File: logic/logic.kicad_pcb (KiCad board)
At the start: 2 copper layers, 27 parts, among them J1 DIN41612_03x32_ABC, J2 Conn_02x05_Odd_Even, U1 TPIC6595, U2 TPIC6595, U3 TPIC6595, U4 TPIC6595, U5 TPIC6595, U6 TPIC6595, U7 TPIC6595, U8 TPIC6595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

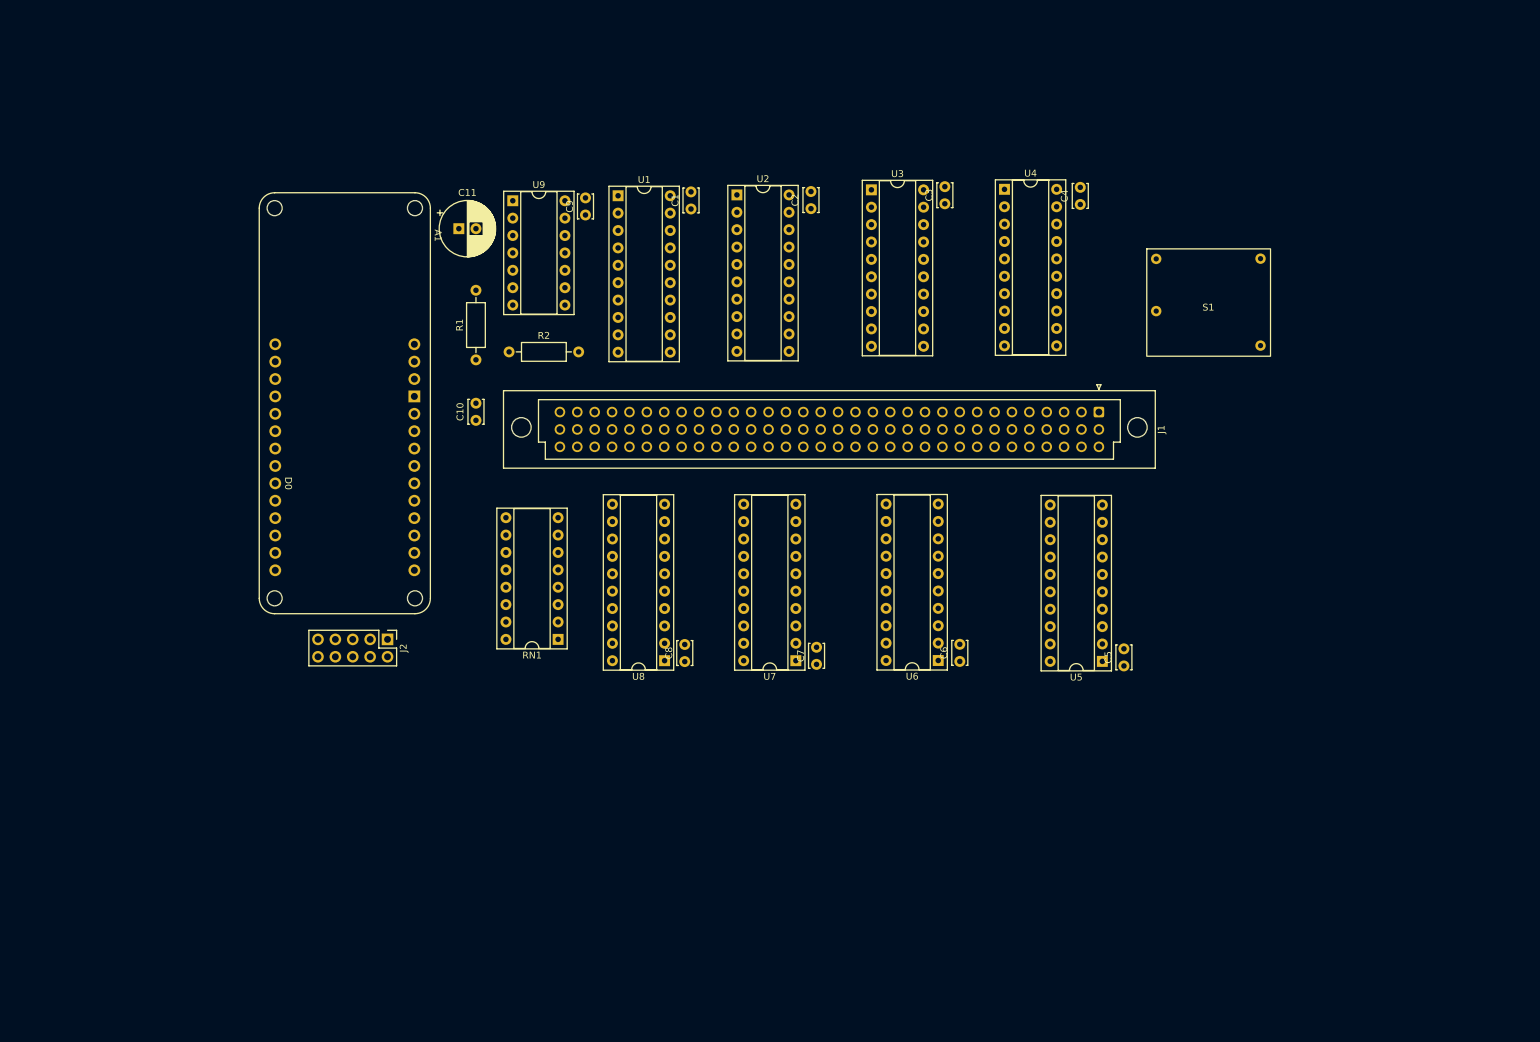
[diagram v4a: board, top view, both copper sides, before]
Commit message: Add low voltage supply to logic board
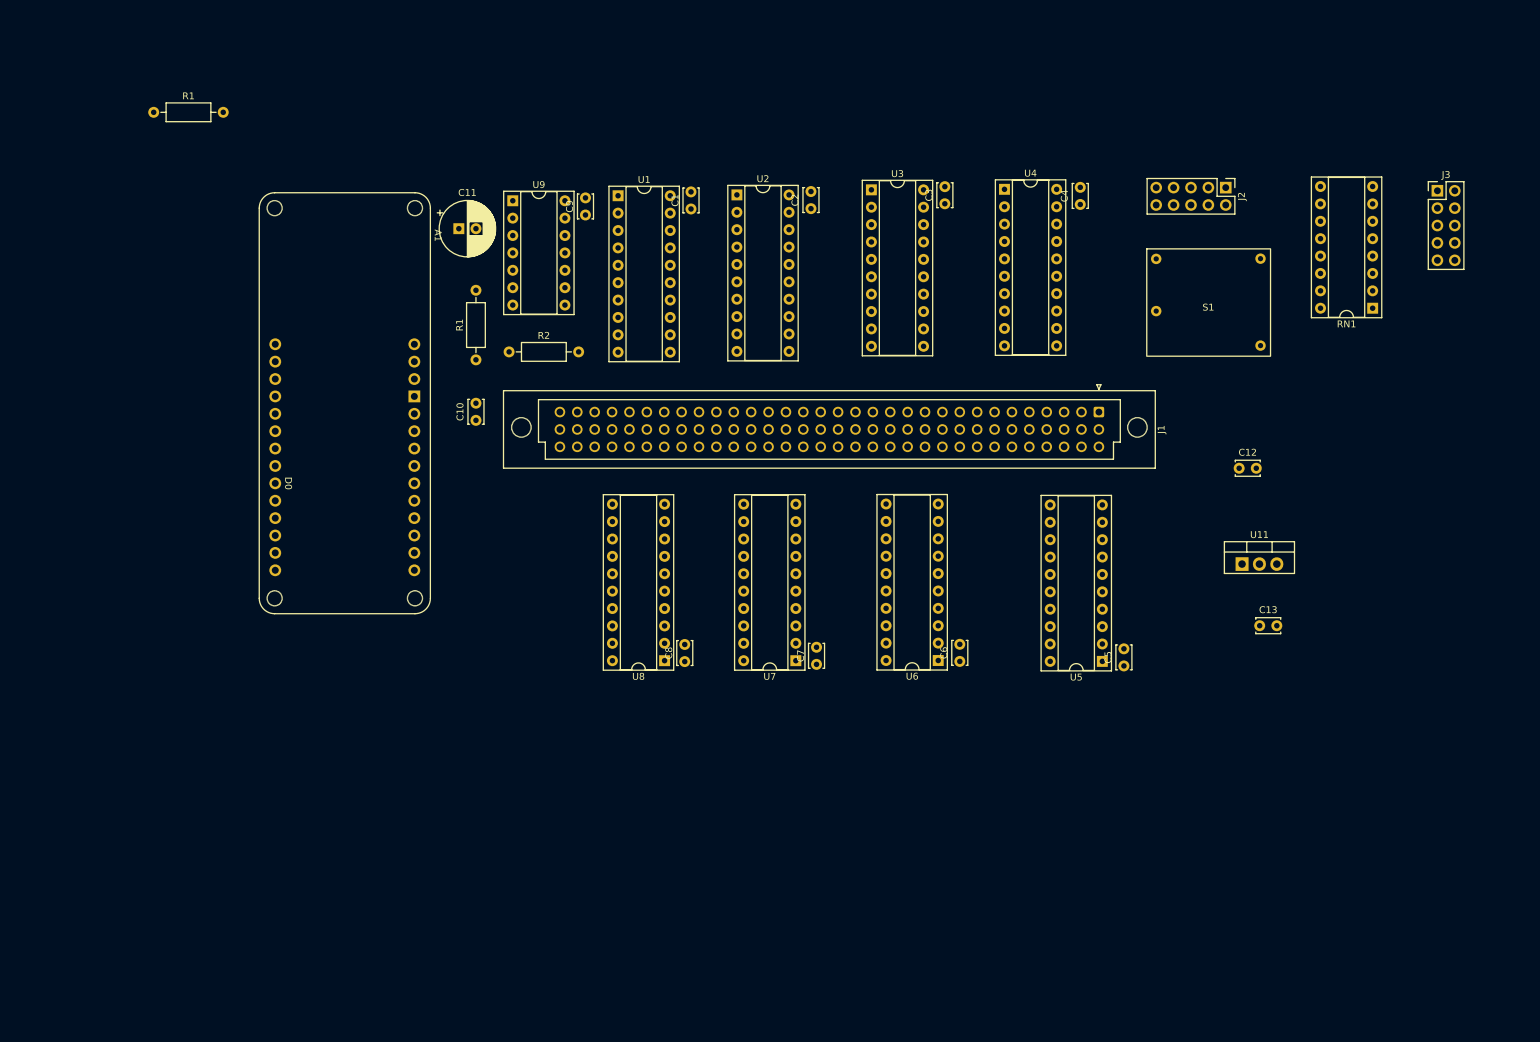
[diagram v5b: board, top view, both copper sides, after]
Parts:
- added C12: C, Capacitor_THT:C_Disc_D3.4mm_W2.1mm_P2.50mm, F.Cu at (214.5, 79.0)
- added C13: C, Capacitor_THT:C_Disc_D3.4mm_W2.1mm_P2.50mm, F.Cu at (217.5, 102.0)
- added J3: Conn_02x05_Odd_Even, Connector_PinHeader_2.54mm:PinHeader_2x05_P2.54mm_Vertical, F.Cu at (243.5, 38.5)
- added R1: R, Resistor_THT:R_Axial_DIN0207_L6.3mm_D2.5mm_P10.16mm_Horizontal, F.Cu at (55.9, 27.0)
- added U11: LM7805_TO220, Package_TO_SOT_THT:TO-220-3_Vertical, F.Cu at (214.9, 93.0)
- moved J2 139.1 mm to (212.5, 38.0)
- moved RN1 128.5 mm to (234.0, 55.6)
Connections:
- A1 pad 5V: unconnected-(A1-Pad5V) -> VCC
- A1 pad D0: Net-(RN1-R8.2) -> Net-(RN1-R6.1)
- A1 pad D1: Net-(RN1-R7.2) -> Net-(RN1-R5.1)
- A1 pad D2: Net-(RN1-R6.2) -> Net-(RN1-R4.1)
- A1 pad D3: Net-(RN1-R5.2) -> Net-(RN1-R3.1)
- A1 pad D4: Net-(RN1-R4.2) -> Net-(RN1-R2.1)
- A1 pad D5: Net-(RN1-R3.2) -> Net-(RN1-R1.1)
- A1 pad VIN: VCC -> LV_REG
- J1 pad a1: VCC -> unconnected-(J1-Pin_a1-Pada1)
- J1 pad a2: VCC -> unconnected-(J1-Pin_a2-Pada2)
- J1 pad b10: GND -> Net-(J1-Pin_b1)
- J1 pad b11: GND -> Net-(J1-Pin_b1)
- J1 pad b12: GND -> Net-(J1-Pin_b1)
- J1 pad b13: GND -> Net-(J1-Pin_b1)
- J1 pad b14: GND -> Net-(J1-Pin_b1)
- J1 pad b15: GND -> Net-(J1-Pin_b1)
- J1 pad b16: GND -> Net-(J1-Pin_b1)
- J1 pad b17: GND -> Net-(J1-Pin_b1)
- J1 pad b18: GND -> Net-(J1-Pin_b1)
- J1 pad b19: GND -> Net-(J1-Pin_b1)
- J1 pad b20: GND -> Net-(J1-Pin_b1)
- J1 pad b21: GND -> Net-(J1-Pin_b1)
- J1 pad b22: GND -> Net-(J1-Pin_b1)
- J1 pad b23: GND -> Net-(J1-Pin_b1)
- J1 pad b24: GND -> Net-(J1-Pin_b1)
- J1 pad b25: Net-(J1-Pin_b25) -> Net-(J1-Pin_b1)
- J1 pad b26: Net-(J1-Pin_b26) -> Net-(J1-Pin_b1)
- J1 pad b27: Net-(J1-Pin_b27) -> Net-(J1-Pin_b1)
- J1 pad b28: Net-(J1-Pin_b28) -> Net-(J1-Pin_b1)
- J1 pad b29: Net-(J1-Pin_b29) -> Net-(J1-Pin_b1)
- J1 pad b30: Net-(J1-Pin_b30) -> Net-(J1-Pin_b1)
- J1 pad b31: Net-(J1-Pin_b31) -> Net-(J1-Pin_b1)
- J1 pad b32: Net-(J1-Pin_b32) -> Net-(J1-Pin_b1)
- J1 pad b8: GND -> Net-(J1-Pin_b1)
- J1 pad b9: GND -> Net-(J1-Pin_b1)
- J1 pad c31: GND -> unconnected-(J1-Pin_c31-Padc31)
- J1 pad c32: GND -> unconnected-(J1-Pin_c32-Padc32)
- RN1 pad 1: Net-(J1-Pin_b25) -> Net-(RN1-R1.1)
- RN1 pad 10: Net-(RN1-R7.2) -> unconnected-(RN1-R7.2-Pad10)
- RN1 pad 11: Net-(RN1-R6.2) -> Net-(J3-Pin_6)
- RN1 pad 12: Net-(RN1-R5.2) -> Net-(J3-Pin_4)
- RN1 pad 13: Net-(RN1-R4.2) -> Net-(J3-Pin_2)
- RN1 pad 14: Net-(RN1-R3.2) -> Net-(J3-Pin_1)
- RN1 pad 15: unconnected-(RN1-R2.2-Pad15) -> Net-(J3-Pin_3)
- RN1 pad 16: unconnected-(RN1-R1.2-Pad16) -> Net-(J3-Pin_5)
- RN1 pad 2: Net-(J1-Pin_b26) -> Net-(RN1-R2.1)
- RN1 pad 3: Net-(J1-Pin_b27) -> Net-(RN1-R3.1)
- RN1 pad 4: Net-(J1-Pin_b28) -> Net-(RN1-R4.1)
- RN1 pad 5: Net-(J1-Pin_b29) -> Net-(RN1-R5.1)
- RN1 pad 6: Net-(J1-Pin_b30) -> Net-(RN1-R6.1)
- RN1 pad 7: Net-(J1-Pin_b31) -> unconnected-(RN1-R7.1-Pad7)
- RN1 pad 8: Net-(J1-Pin_b32) -> unconnected-(RN1-R8.1-Pad8)
- RN1 pad 9: Net-(RN1-R8.2) -> unconnected-(RN1-R8.2-Pad9)

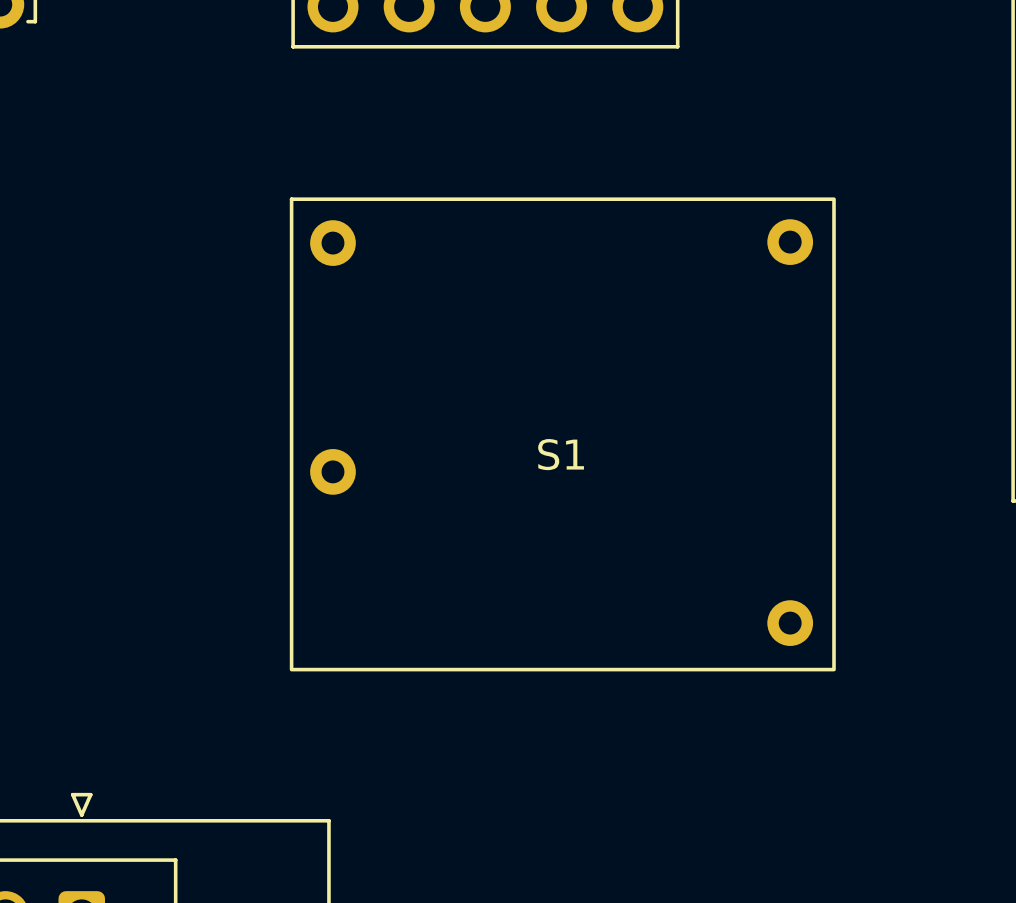
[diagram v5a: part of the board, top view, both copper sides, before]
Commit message: Finally figure out how to attach nets to the NCH8200.
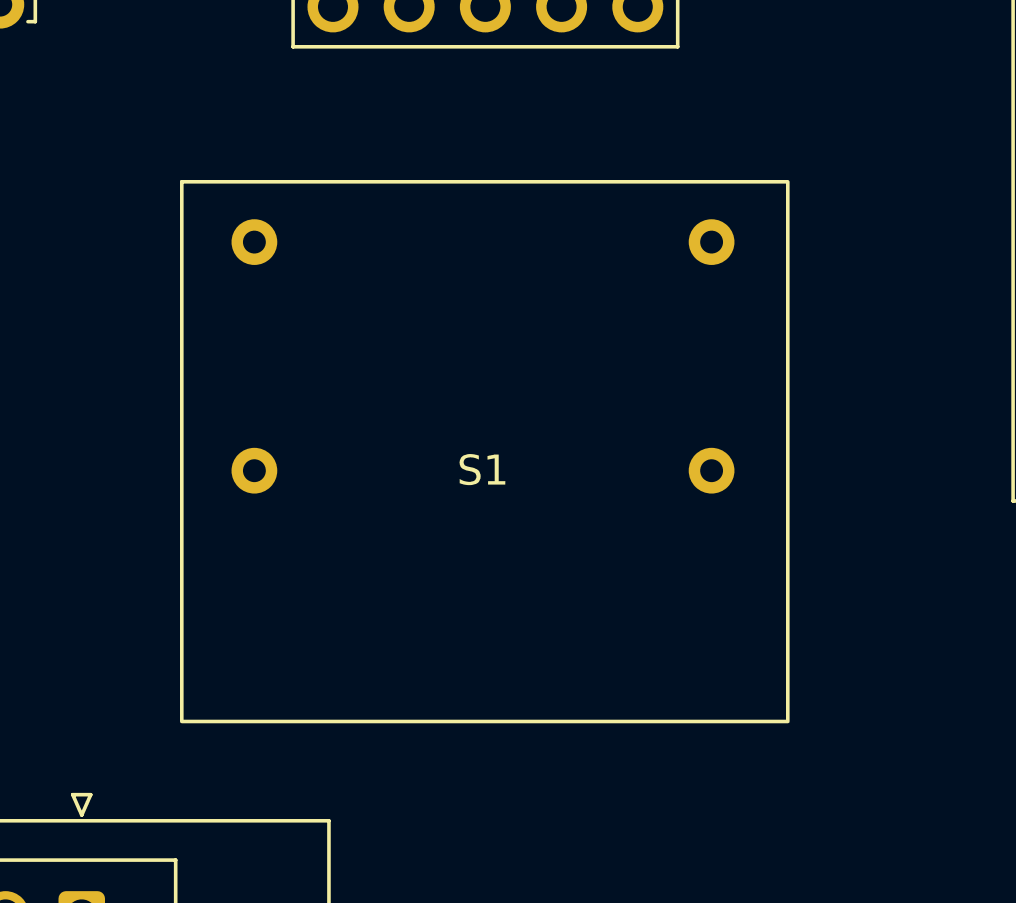
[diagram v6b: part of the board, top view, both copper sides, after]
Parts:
- moved S1 3.65 mm to (207.4, 53.5)
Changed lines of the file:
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@@
 	(net 122 "unconnected-(RN1-R8.1-Pad8)")
 	(net 123 "unconnected-(RN1-R7.1-Pad7)")
-	(footprint "NixComp:NCH8200HV"
-		(layer "F.Cu")
-		(at 210 56)
-		(property "Reference" "S1"
-			(at 0 -0.5 0)
-			(unlocked yes)
-			(layer "F.SilkS")
-			(effects
-				(font
-					(size 1 1)
-					(thickness 0.15)
-				)
-			)
-		)
-		(property "Value" "~"
-			(at 0 1 0)
-			(unlocked yes)
-			(layer "F.Fab")
-			(effects
-				(font
-					(size 1 1)
-					(thickness 0.15)
-				)
-			)
-		)
-		(property "Footprint" "NixComp:NCH8200HV"
-			(at 0 0 0)
-			(unlocked yes)
-			(layer "F.Fab")
-			(hide yes)
-			(effects
-				(font
-					(size 1 1)
-					(thickness 0.15)
-				)
-			)
-		)
-		(property "Datasheet" ""
-			(at 0 0 0)
-			(unlocked yes)
-			(layer "F.Fab")
-			(hide yes)
-			(effects
-				(font
-					(size 1 1)
-					(thickness 0.15)
-				)
-			)
-		)
-		(property "Description" ""
-			(at 0 0 0)
-			(unlocked yes)
-			(layer "F.Fab")
-			(hide yes)
-			(effects
-				(font
-					(size 1 1)
-					(thickness 0.15)
-				)
-			)
-		)
-		(sheetname "Root")
-		(sheetfile "logic.kicad_sch")
-		(attr through_hole)
-		(fp_rect
-			(start -9 -9.05)
-			(end 9.08 6.63)
-			(stroke
-				(width 0.12)
-				(type default)
-			)
-			(fill none)
-			(layer "F.SilkS")
-		)
-		(fp_text user "${REFERENCE}"
-			(at 0 2.5 0)
-			(unlocked yes)
-			(layer "F.Fab")
-			(effects
-				(font
-					(size 1 1)
-					(thickness 0.15)
-				)
-			)
-		)
-		(pad "5" thru_hole circle
-			(at -7.62 -7.5876)
-			(size 1.524 1.524)
-			(drill 0.762)
-			(layers "*.Cu" "*.Mask")
-			(remove_unused_layers no)
-		)
-		(pad "6" thru_hole circle
-			(at 7.62 -7.62)
-			(size 1.524 1.524)
-			(drill 0.762)
-			(layers "*.Cu" "*.Mask")
-			(remove_unused_layers no)
-		)
-		(pad "7" thru_hole circle
-			(at -7.62 0.04)
-			(size 1.524 1.524)
-			(drill 0.762)
-			(layers "*.Cu" "*.Mask")
-			(remove_unused_layers no)
-		)
-		(pad "8" thru_hole circle
-			(at 7.62 5.08)
-			(size 1.524 1.524)
-			(drill 0.762)
-			(layers "*.Cu" "*.Mask")
-			(remove_unused_layers no)
-		)
-	)
 	(footprint "Capacitor_THT:C_Disc_D3.4mm_W2.1mm_P2.50mm"
 		(layer "F.Cu")
@@
 		(tags "Through hole pin header THT 2x05 2.54mm double row")
 		(property "Reference" "J3"
-			(at 1.27 -2.33 360)
+			(at 1.27 -2.33 0)
 			(layer "F.SilkS")
 			(effects
@@
 		)
 		(property "Value" "Conn_02x05_Odd_Even"
-			(at 1.27 12.49 360)
+			(at 1.27 12.49 0)
 			(layer "F.Fab")
 			(effects
@@
 		)
 	)
+	(footprint "NixComp:NCH8200HV"
+		(layer "F.Cu")
+		(at 207.38 53.46)
+		(property "Reference" "S1"
+			(at 0 2.54 0)
+			(unlocked yes)
+			(layer "F.SilkS")
+			(effects
+				(font
+					(size 1 1)
+					(thickness 0.15)
+				)
+			)
+		)
+		(property "Value" "~"
+			(at 0 12.7 0)
+			(unlocked yes)
+			(layer "F.Fab")
+			(effects
+				(font
+					(size 1 1)
+					(thickness 0.15)
+				)
+			)
+		)
+		(property "Footprint" "NixComp:NCH8200HV"
+			(at -12.7 10.16 0)
+			(unlocked yes)
+			(layer "F.Fab")
+			(hide yes)
+			(effects
+				(font
+					(size 1 1)
+					(thickness 0.15)
+				)
+			)
+		)
+		(property "Datasheet" ""
+			(at -12.7 10.16 0)
+			(unlocked yes)
+			(layer "F.Fab")
+			(hide yes)
+			(effects
+				(font
+					(size 1 1)
+					(thickness 0.15)
+				)
+			)
+		)
+		(property "Description" ""
+			(at -12.7 10.16 0)
+			(unlocked yes)
+			(layer "F.Fab")
+			(hide yes)
+			(effects
+				(font
+					(size 1 1)
+					(thickness 0.15)
+				)
+			)
+		)
+		(sheetname "Root")
+		(sheetfile "logic.kicad_sch")
+		(attr through_hole)
+		(fp_rect
+			(start -10.039896 -7.089948)
+			(end 10.16 10.899948)
+			(stroke
+				(width 0.12)
+				(type default)
+			)
+			(fill none)
+			(layer "F.SilkS")
+		)
+		(fp_text user "${REFERENCE}"
+			(at 0 15.24 0)
+			(unlocked yes)
+			(layer "F.Fab")
+			(effects
+				(font
+					(size 1 1)
+					(thickness 0.15)
+				)
+			)
+		)
+		(pad "1" thru_hole circle
+			(at -7.62 -5.08)
+			(size 1.524 1.524)
+			(drill 0.762)
+			(layers "*.Cu" "*.Mask")
+			(remove_unused_layers no)
+			(net 62 "VCC")
+			(pinfunction "LV_IN")
+			(pintype "power_in")
+		)
+		(pad "2" thru_hole circle
+			(at -7.62 2.54)
+			(size 1.524 1.524)
+			(drill 0.762)
+			(layers "*.Cu" "*.Mask")
+			(remove_unused_layers no)
+			(net 23 "GND")
+			(pinfunction "LGND")
+			(pintype "power_in")
+		)
+		(pad "3" thru_hole circle
+			(at 7.62 2.54)
+			(size 1.524 1.524)
+			(drill 0.762)
+			(layers "*.Cu" "*.Mask")
+			(remove_unused_layers no)
+			(net 23 "GND")
+			(pinfunction "PGND")
+			(pintype "power_in")
+		)
+		(pad "4" thru_hole circle
+			(at 7.62 -5.08)
+			(size 1.524 1.524)
+			(drill 0.762)
+			(layers "*.Cu" "*.Mask")
+			(remove_unused_layers no)
+			(net 92 "Net-(J1-Pin_b1)")
+			(pinfunction "HV_OUT")
+			(pintype "power_out")
+		)
+	)
 	(footprint "Package_DIP:DIP-20_W7.62mm_Socket"
 		(layer "F.Cu")
@@
 		(tags "THT DIP DIL PDIP 2.54mm 7.62mm 300mil Socket")
 		(property "Reference" "RN1"
-			(at 3.81 -2.33 360)
+			(at 3.81 -2.33 0)
 			(layer "F.SilkS")
 			(effects
@@
 		)
 		(property "Value" "R_Pack08"
-			(at -1.2192 45.8724 360)
+			(at -1.2192 45.8724 0)
 			(layer "F.Fab")
 			(effects
@@
 		)
 		(fp_text user "${REFERENCE}"
-			(at 3.81 8.89 360)
+			(at 3.81 8.89 0)
 			(layer "F.Fab")
 			(effects

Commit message: Commit older work
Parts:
- added J4: Conn_02x05_Odd_Even, Connector_PinHeader_2.54mm:PinHeader_2x05_P2.54mm_Vertical, F.Cu at (101.7, 87.1)
- moved R1 71.1 mm to (100.1, 82.7), turned to 90 degrees
- moved C10 2.33 mm to (103.0, 69.7)

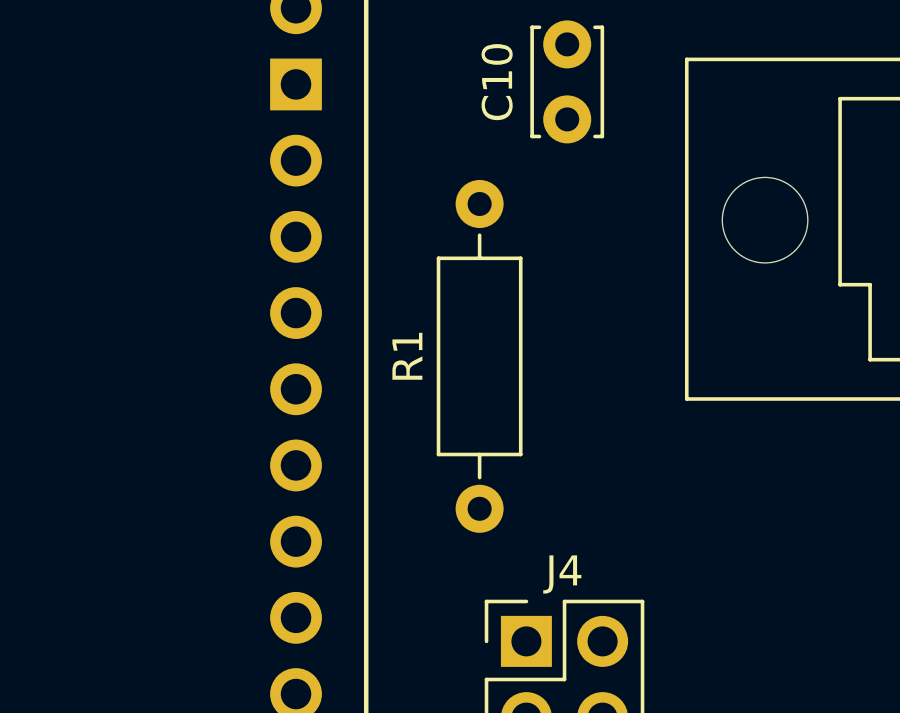
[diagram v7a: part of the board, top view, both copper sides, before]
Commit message: Fix a problem with R1 on PCB
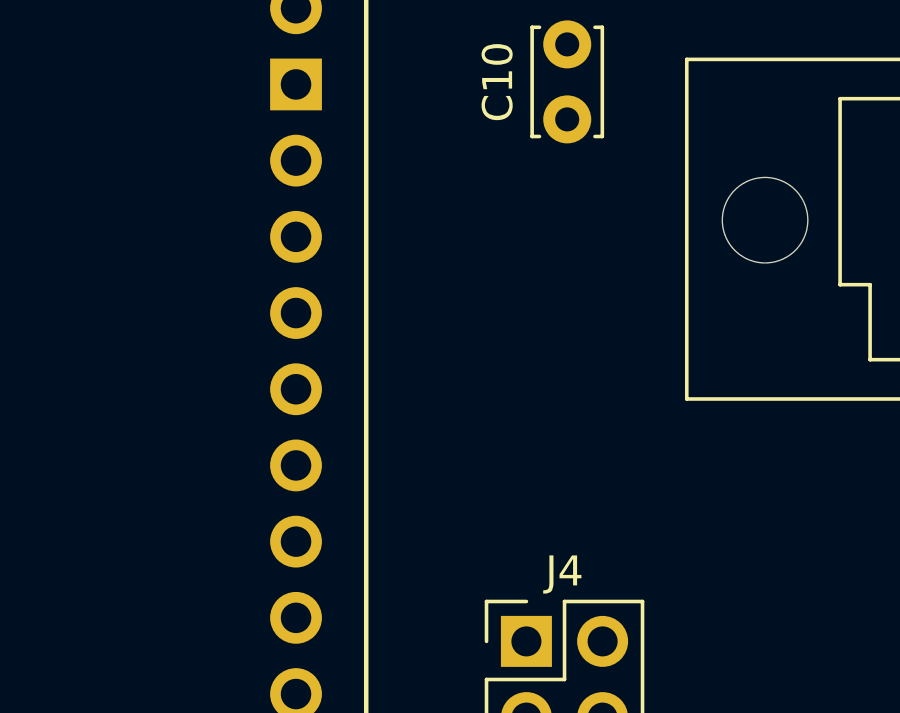
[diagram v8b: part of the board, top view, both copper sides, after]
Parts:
- removed the R1 at (100.1, 82.7)
